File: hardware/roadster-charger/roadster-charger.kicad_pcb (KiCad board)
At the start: 4 copper layers, 74.4 x 50.2 mm, 108 parts, among them J1 USB4505-03-0-A, J2 USB4505-03-0-A, J3 54-00166, Q1 CSD19532Q5B, U1 MPM3606AGQV-P, U10 DAC70501ZDQFT, U11 PI3740-00-LGIZ, U2 ESP32-C3-MINI-1, U3 INA168, U4 OPA340NA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

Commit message: connect inductor mounting pin to large ground area
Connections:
- L1 pad 3: unconnected-(L1-MNT-Pad3) -> GND
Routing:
- net GND: vias 153 -> 160

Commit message: increase input capacitance for buck / boost
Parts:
- C18, C19, C20, C21, C22: value 2.2uF -> 10uF
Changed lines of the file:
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@@
 			)
 		)
-		(property "Value" "2.2uF"
+		(property "Value" "10uF"
 			(at 0 2.3 90)
 			(layer "F.Fab")
@@
 			)
 		)
-		(property "MPN" "GRM32ER72A225KA35L"
+		(property "MPN" "CL32B106KBVVPLE"
 			(at 0 0 90)
 			(unlocked yes)
@@
 			)
 		)
-		(property "Value" "2.2uF"
+		(property "Value" "10uF"
 			(at 0 2.3 90)
 			(layer "F.Fab")
@@
 			)
 		)
-		(property "MPN" "GRM32ER72A225KA35L"
+		(property "MPN" "CL32B106KBVVPLE"
 			(at 0 0 -90)
 			(unlocked yes)
@@
 			)
 		)
-		(property "Value" "2.2uF"
+		(property "Value" "10uF"
 			(at 0 2.3 90)
 			(layer "F.Fab")
@@
 			)
 		)
-		(property "MPN" "GRM32ER72A225KA35L"
+		(property "MPN" "CL32B106KBVVPLE"
 			(at 0 0 90)
 			(unlocked yes)
@@
 			)
 		)
-		(property "Value" "2.2uF"
+		(property "Value" "10uF"
 			(at 0 2.3 90)
 			(layer "F.Fab")
@@
 			)
 		)
-		(property "MPN" "GRM32ER72A225KA35L"
+		(property "MPN" "CL32B106KBVVPLE"
 			(at 0 0 -90)
 			(unlocked yes)
@@
 			)
 		)
-		(property "Value" "2.2uF"
+		(property "Value" "10uF"
 			(at 0 2.3 90)
 			(layer "F.Fab")
@@
 			)
 		)
-		(property "MPN" "GRM32ER72A225KA35L"
+		(property "MPN" "CL32B106KBVVPLE"
 			(at 0 0 90)
 			(unlocked yes)

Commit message: clean up USB
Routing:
- net /USB_DM: track 26.7 -> 25.6 mm
- net /USB_DP: track 25.4 -> 24.7 mm
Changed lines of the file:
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@@
-	)
-	(segment
-		(start 183.5 150.165686)
-		(end 184.334314 151)
-		(width 0.2)
-		(layer "F.Cu")
-		(net 17)
 	)
 	(segment
@@
 	)
 	(segment
+		(start 184.334314 145.8)
+		(end 183.7 146.434314)
+		(width 0.2)
+		(layer "F.Cu")
+		(net 17)
+	)
+	(segment
+		(start 190.8 145.8)
+		(end 184.334314 145.8)
+		(width 0.2)
+		(layer "F.Cu")
+		(net 17)
+	)
+	(segment
+		(start 191 143.85)
+		(end 191.65 143.85)
+		(width 0.2)
+		(layer "F.Cu")
+		(net 17)
+	)
+	(segment
+		(start 183.7 149.3)
+		(end 185.4 151)
+		(width 0.2)
+		(layer "F.Cu")
+		(net 17)
+	)
+	(segment
+		(start 190.1995 138.45)
+		(end 190.2 138.4495)
+		(width 0.2)
+		(layer "F.Cu")
+		(net 17)
+	)
+	(segment
 		(start 191.7 144.9)
 		(end 190.8 145.8)
@@
 	)
 	(segment
-		(start 191.7 144.9)
-		(end 191.7 143.8)
-		(width 0.2)
-		(layer "F.Cu")
-		(net 17)
-	)
-	(segment
-		(start 191 143.85)
-		(end 191.65 143.85)
-		(width 0.2)
-		(layer "F.Cu")
-		(net 17)
-	)
-	(segment
-		(start 184.334314 145.8)
-		(end 183.5 146.634314)
-		(width 0.2)
-		(layer "F.Cu")
-		(net 17)
-	)
-	(segment
-		(start 183.5 146.634314)
-		(end 183.5 150.165686)
-		(width 0.2)
-		(layer "F.Cu")
-		(net 17)
-	)
-	(segment
-		(start 190.1995 138.45)
-		(end 190.2 138.4495)
-		(width 0.2)
-		(layer "F.Cu")
-		(net 17)
-	)
-	(segment
 		(start 191.7 143.8)
 		(end 191.7 143.225)
@@
 	)
 	(segment
+		(start 183.7 146.434314)
+		(end 183.7 149.3)
+		(width 0.2)
+		(layer "F.Cu")
+		(net 17)
+	)
+	(segment
 		(start 191.7 143.225)
 		(end 191.725 143.2)
@@
 	)
 	(segment
-		(start 190.8 145.8)
-		(end 184.334314 145.8)
-		(width 0.2)
-		(layer "F.Cu")
-		(net 17)
-	)
-	(segment
-		(start 184.334314 151)
+		(start 185.4 151)
 		(end 185.7 151)
 		(width 0.2)
@@
 		(net 17)
 	)
+	(segment
+		(start 191.7 143.8)
+		(end 191.7 144.9)
+		(width 0.2)
+		(layer "F.Cu")
+		(net 17)
+	)
 	(via
 		(at 191.725 143.2)
@@
 	)
 	(segment
-		(start 190.7495 139.4495)
+		(start 190.8495 139.4495)
 		(end 190.2 139.4495)
-		(width 0.25)
-		(layer "B.Cu")
-		(net 17)
-	)
-	(segment
-		(start 191.725 143.2)
-		(end 191.725 140.425)
-		(width 0.25)
+		(width 0.2)
+		(layer "B.Cu")
+		(net 17)
+	)
+	(segment
+		(start 191.7 140.3)
+		(end 190.8495 139.4495)
+		(width 0.2)
+		(layer "B.Cu")
+		(net 17)
+	)
+	(segment
+		(start 191.7 143.175)
+		(end 191.7 140.3)
+		(width 0.2)
 		(layer "B.Cu")
 		(net 17)
@@
 	)
 	(segment
-		(start 191.725 140.425)
-		(end 190.7495 139.4495)
-		(width 0.25)
-		(layer "B.Cu")
-		(net 17)
-	)
-	(segment
-		(start 183.9 149.9)
-		(end 184.2 150.2)
+		(start 191.725 143.2)
+		(end 191.7 143.175)
+		(width 0.2)
+		(layer "B.Cu")
+		(net 17)
+	)
+	(segment
+		(start 184.1 149)
+		(end 185.3 150.2)
 		(width 0.2)
 		(layer "F.Cu")
@@
 	)
 	(segment
+		(start 192.2245 143.8)
+		(end 192.2245 144.9755)
+		(width 0.2)
+		(layer "F.Cu")
+		(net 18)
+	)
+	(segment
+		(start 184.5 146.2)
+		(end 184.1 146.6)
+		(width 0.2)
+		(layer "F.Cu")
+		(net 18)
+	)
+	(segment
 		(start 190.8 138.4)
-		(end 191.3 138.4)
-		(width 0.2)
-		(layer "F.Cu")
-		(net 18)
-	)
-	(segment
-		(start 184.2 150.2)
-		(end 185.7 150.2)
+		(end 190.8 138.82)
+		(width 0.2)
+		(layer "F.Cu")
+		(net 18)
+	)
+	(segment
+		(start 184.1 146.6)
+		(end 184.1 149)
 		(width 0.2)
 		(layer "F.Cu")
@@
 	)
 	(segment
-		(start 184.5 146.2)
-		(end 183.9 146.8)
-		(width 0.2)
-		(layer "F.Cu")
-		(net 18)
-	)
-	(segment
 		(start 191 146.2)
 		(end 184.5 146.2)
@@
 	)
 	(segment
-		(start 190.8 138.4)
-		(end 190.8 138.82)
-		(width 0.2)
-		(layer "F.Cu")
-		(net 18)
-	)
-	(segment
-		(start 192.2245 143.8)
-		(end 192.2245 144.9755)
-		(width 0.2)
-		(layer "F.Cu")
-		(net 18)
-	)
-	(segment
-		(start 183.9 146.8)
-		(end 183.9 149.9)
+		(start 185.3 150.2)
+		(end 185.7 150.2)
 		(width 0.2)
 		(layer "F.Cu")
@@
 	)
 	(via
-		(at 191.3 138.4)
-		(size 0.4)
-		(drill 0.2)
-		(layers "F.Cu" "B.Cu")
-		(net 18)
-	)
-	(segment
-		(start 192.2245 143.8)
-		(end 192.2245 139.3245)
-		(width 0.2)
-		(layer "B.Cu")
-		(net 18)
-	)
-	(segment
-		(start 192.2245 139.3245)
-		(end 191.3 138.4)
-		(width 0.2)
-		(layer "B.Cu")
+		(at 190.8 138.4)
+		(size 0.4)
+		(drill 0.2)
+		(layers "F.Cu" "B.Cu")
+		(net 18)
+	)
+	(segment
+		(start 190.8 138.8)
+		(end 192.2245 140.2245)
+		(width 0.2)
+		(layer "B.Cu")
+		(net 18)
+	)
+	(segment
+		(start 190.8 138.4)
+		(end 190.8 138.8)
+		(width 0.2)
+		(layer "B.Cu")
+		(net 18)
+	)
+	(segment
+		(start 192.2245 140.2245)
+		(end 192.2245 143.8)
+		(width 0.2)
+		(layer "B.Cu")

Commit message: Correct resistor from 1206 to 0603
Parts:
- R25: value 25K -> 25.5K
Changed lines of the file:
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@@
 			)
 		)
-		(property "Value" "25K"
+		(property "Value" "25.5K"
 			(at 0 1.43 90)
 			(layer "F.Fab")
@@
 			)
 		)
-		(property "MPN" "RT1206BRD0725KL"
+		(property "MPN" "RT0603BRD0725K5L"
 			(at 0 0 -90)
 			(unlocked yes)

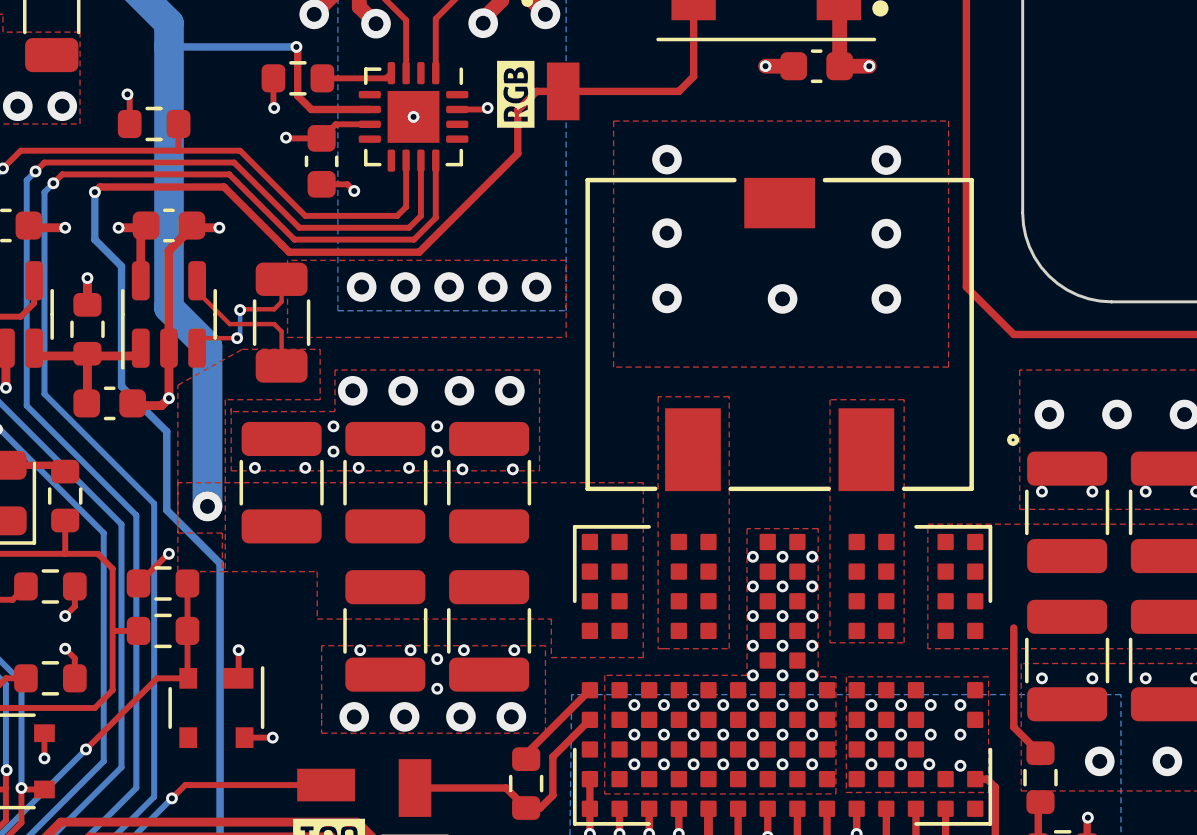
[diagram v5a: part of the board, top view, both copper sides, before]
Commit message: Small updates from Rev 2 production run
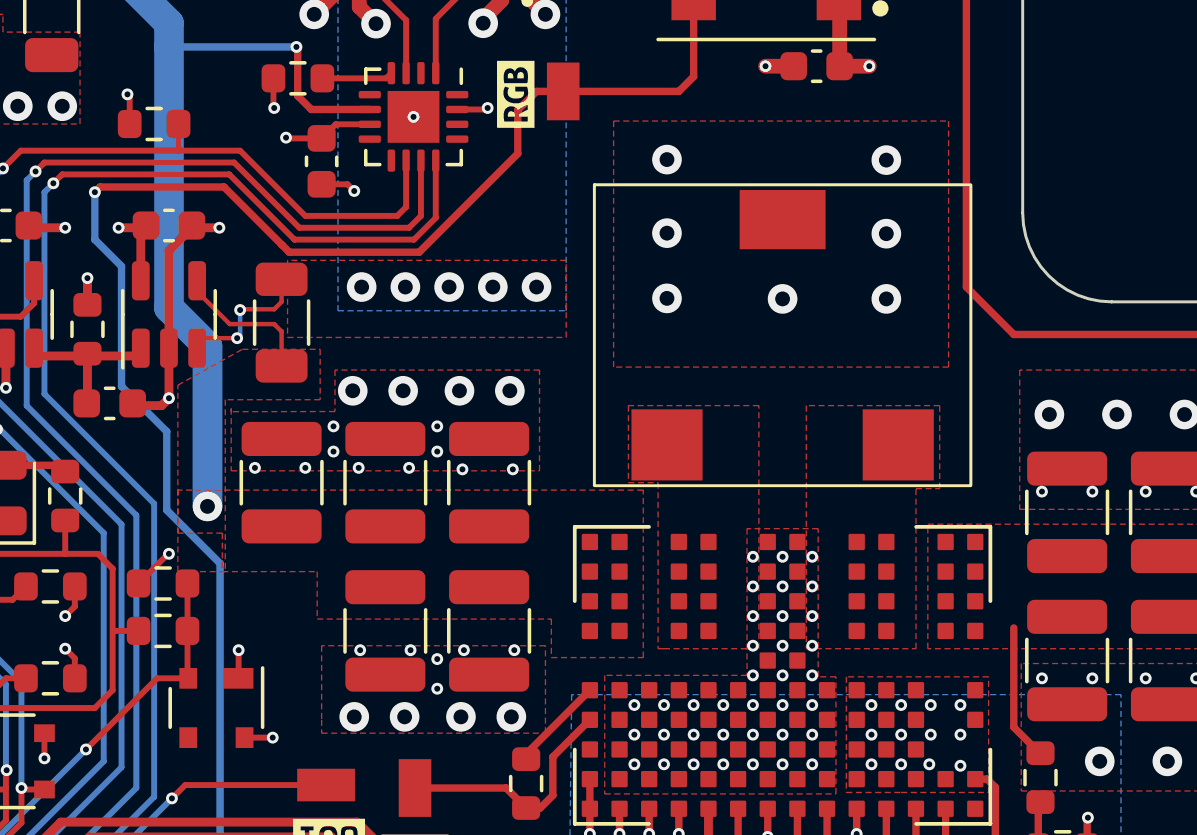
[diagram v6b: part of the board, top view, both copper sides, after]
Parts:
- U6: value LM75B -> LM75BD,118

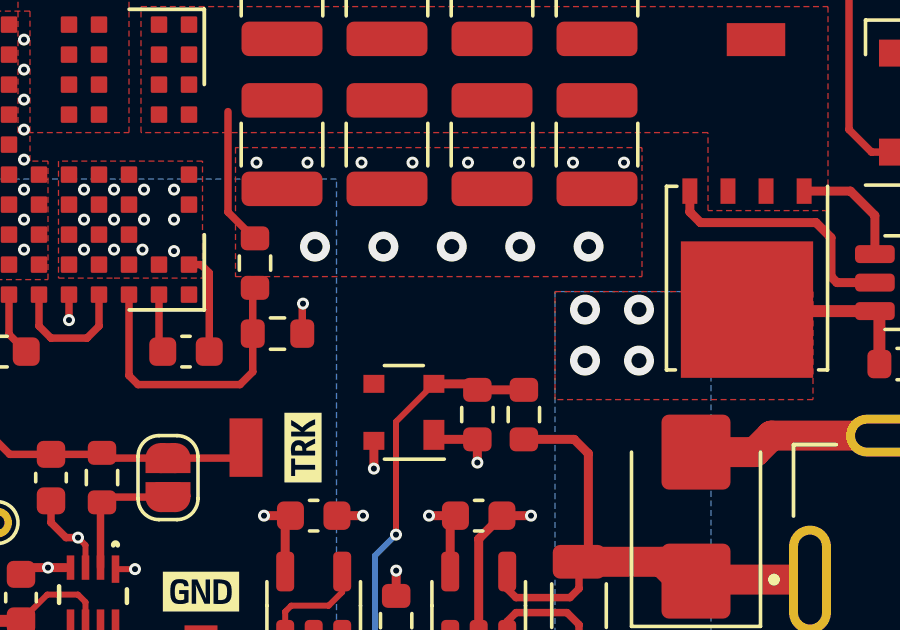
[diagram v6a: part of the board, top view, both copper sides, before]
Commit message: add fan connection points
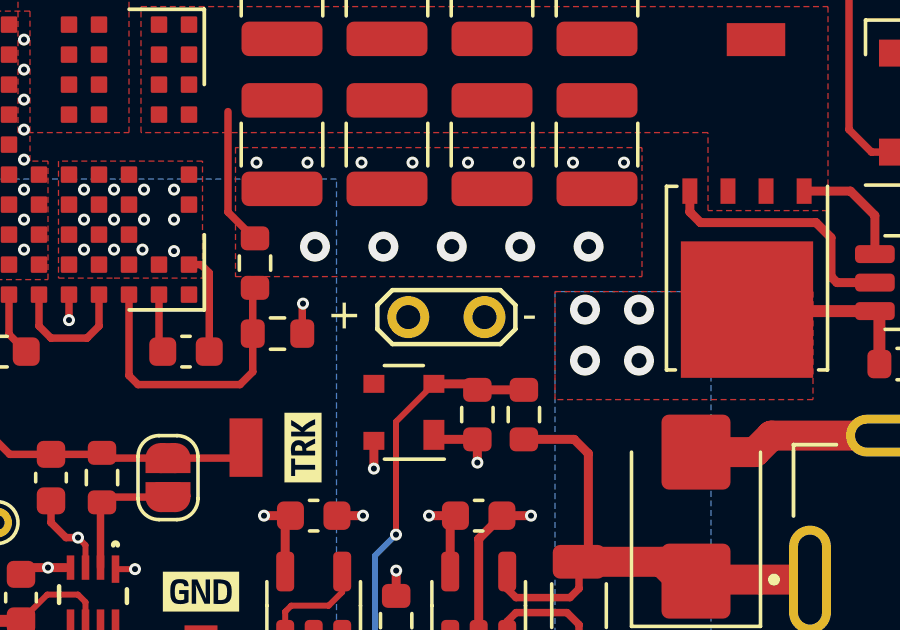
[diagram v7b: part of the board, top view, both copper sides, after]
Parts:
- added TP13: ~, TestPoint:TestPoint_2Pads_Pitch2.54mm_Drill0.8mm, F.Cu at (234.2, 145.2)
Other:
- board text added: "+"
- board text added: "-"
